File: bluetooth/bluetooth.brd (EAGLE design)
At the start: 59.7 x 53.3 mm, 6 parts

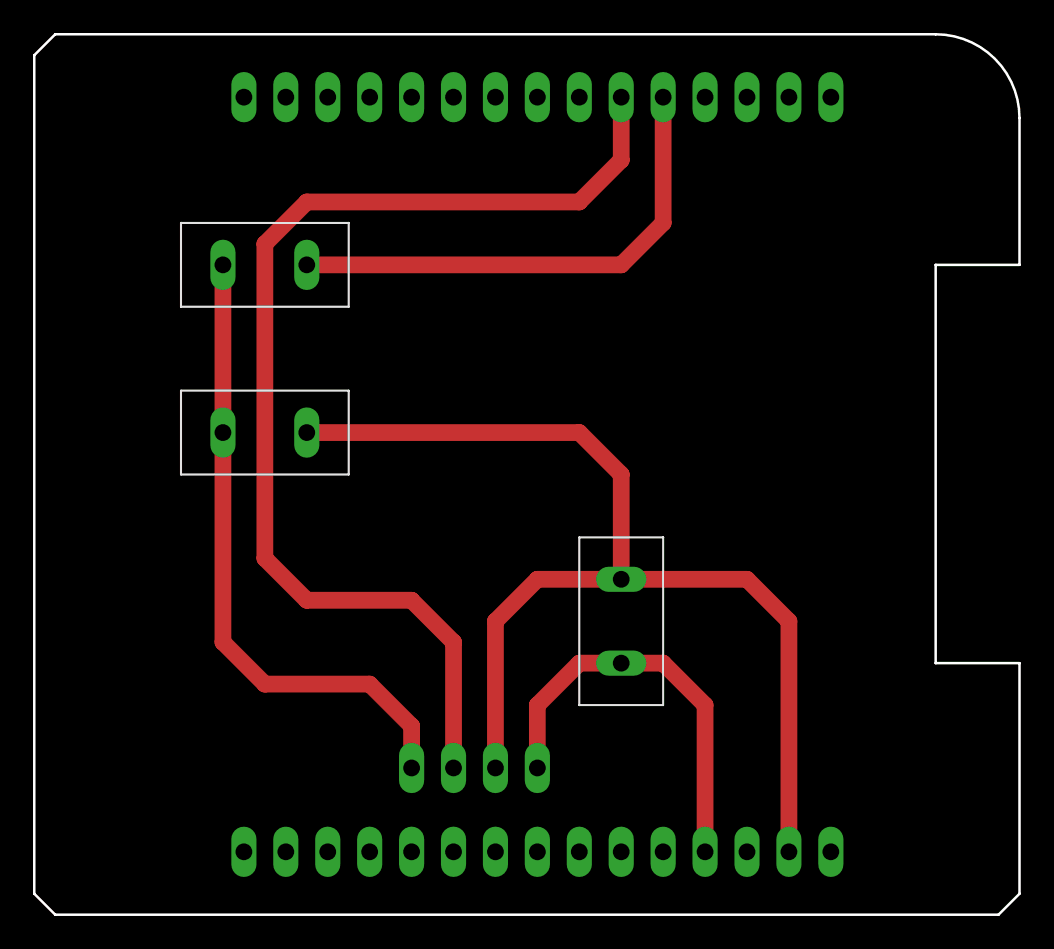
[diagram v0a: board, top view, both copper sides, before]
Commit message: Updated Boards for New Configuration
Bluetooth board has been rearranged to accommodate board slot-in
Motor Control Board flipped to be in the right spot
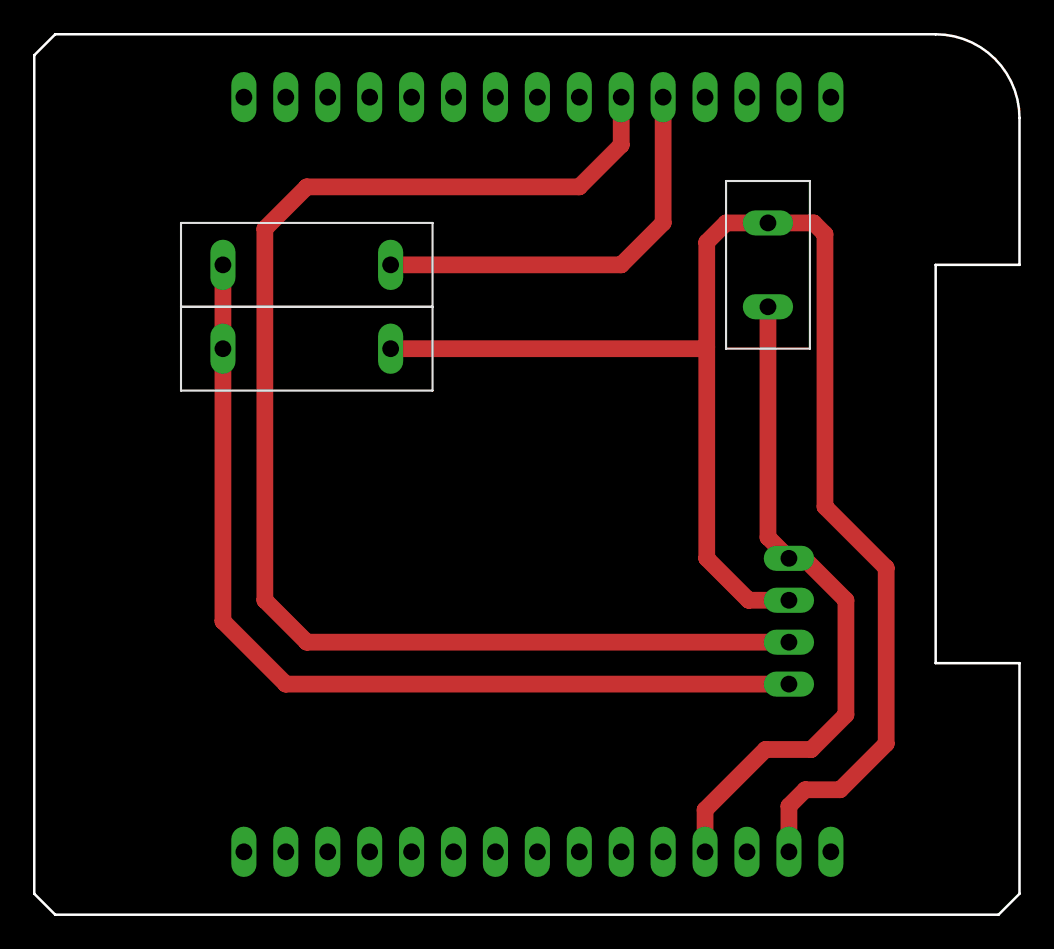
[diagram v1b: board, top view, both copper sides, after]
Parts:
- U$3, U$4: device RC Car:RESISTOR -> rc_car:RESISTOR
- moved POWER 23.3 mm to (44.5, 39.4)
- moved U$6 19.8 mm to (45.7, 21.6), turned to 270 degrees
- moved U$4 5.68 mm to (16.5, 34.3)
- moved U$3 2.54 mm to (16.5, 39.4)
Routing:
- net GND: track 69.2 -> 95.1 mm
- net RX: track 38.9 -> 57.5 mm
- net 5V: track 25.0 -> 40.7 mm
- net D03: track 67.7 -> 81.9 mm
- net D02: track 30.3 -> 25.2 mm
